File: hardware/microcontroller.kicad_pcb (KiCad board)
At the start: 2 copper layers, 50.8 x 78.7 mm, 77 parts, among them J5 1x2 jumper right-angle, J6 RJ45_Amphenol_RJMG1BD3B8K1ANR, J7 1x2 jumper right-angle, U1 W5500, U10 register file, U11 register file, U12 3.3V <=> 5V, U13 flip-flop, U14 3.3V <=> 5V, U15 decoder, U16 3.3V <=> 5V, U17 decoder, U2 3.3V <=> 5V, U3 counter, U4 counter, U5 counter, U6 counter, U7 counter, U8 shift register, U9 shift register, Y1 25MHz

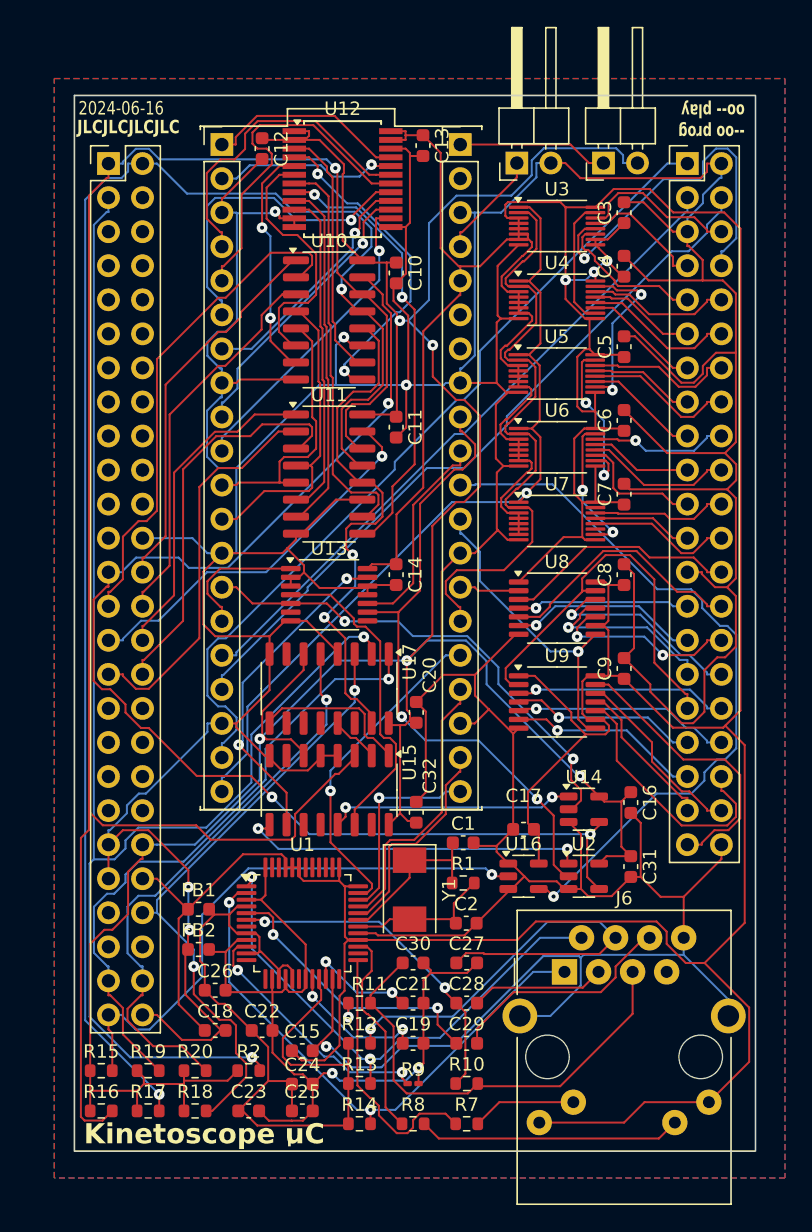
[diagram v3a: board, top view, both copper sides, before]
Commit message: Revise microcontroller board based on latest cart board improvements
 - Update comments
 - Segregate the Ethernet module's power supply so it can be
   disconnected if something goes wrong in a prototype
 - Update board setup to match latest cart board
 - Remove unnecessary level-shifter
 - Fix address decoder to non-latching version
 - Fix address decoder output assignment
 - Consolidate buffer ICs in register file
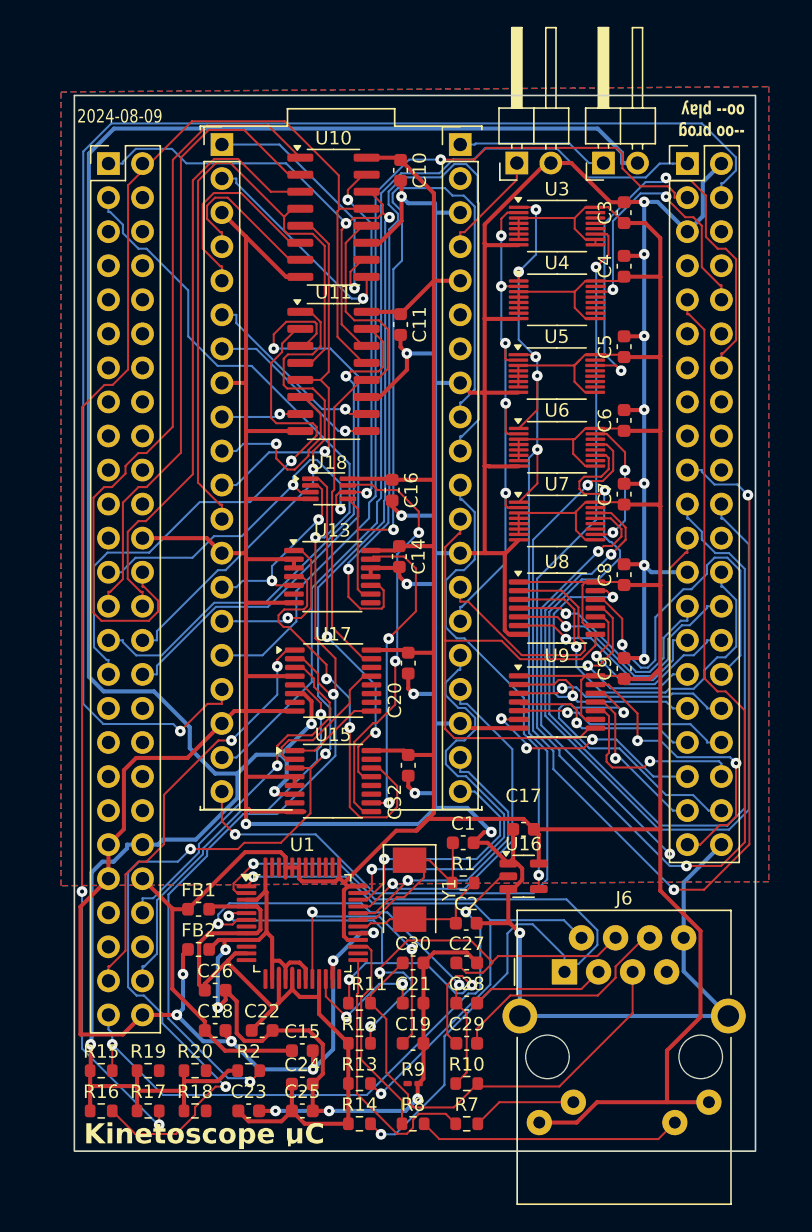
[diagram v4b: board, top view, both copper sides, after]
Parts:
- removed C12, C13, C31: 22nF, Capacitor_SMD:C_0603_1608Metric
- removed U12: 3.3V <=> 5V, Package_SO:SSOP-24_5.3x8.2mm_P0.65mm
- removed U14, U2: 3.3V <=> 5V, Package_TO_SOT_SMD:SOT-23-5
- added U18: 74LVC2G125, Package_SO:VSSOP-8_2.3x2mm_P0.5mm, F.Cu at (37.7, 48.6)
- U10, U11: value register file -> 74HC670
- U13: value flip-flop -> 74AHC74
- U15, U17: value decoder -> 74LVC138; footprint Package_SO:SO-16_3.9x9.9mm_P1.27mm -> Package_SO:TSSOP-16_4.4x5mm_P0.65mm
- U16: value 3.3V <=> 5V -> 74LV1T125
- U3, U4, U5, U6, U7: value counter -> 74LV163
- U8, U9: value shift register -> 74LV164
- moved C16 29.3 mm to (42.4, 48.7)
- moved C11 7.66 mm to (43.1, 36.4)
- moved U11 7.66 mm to (38.1, 39.9)
- moved C10 7.66 mm to (43.1, 24.9)
- moved U10 7.66 mm to (38.1, 28.4)
- moved C20 3.72 mm to (43.6, 61.6), turned to -90 degrees
- moved C32 3.55 mm to (43.6, 69.3), turned to -90 degrees
- moved C14 1.37 mm to (43.0, 53.7)
- moved U13 1.37 mm to (38.0, 55.2)
- moved U15 0.73 mm to (38.0, 70.4), turned to 0 degrees
- moved U17 0.67 mm to (38.0, 62.9), turned to 0 degrees
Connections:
- C10 pad 1: +5V -> +3.3V
- C11 pad 1: +5V -> +3.3V
- C16 pad 1: +5V -> +3.3V
- C20 pad 1: +5V -> +3.3V
- C32 pad 1: +5V -> +3.3V
- U10 pad 10: /register-file-internal/D_MID0 -> /REG_R_D0
- U10 pad 16: +5V -> +3.3V
- U10 pad 6: /register-file-internal/D_MID3 -> /REG_R_D3
- U10 pad 7: /register-file-internal/D_MID2 -> /REG_R_D2
- U10 pad 9: /register-file-internal/D_MID1 -> /REG_R_D1
- U11 pad 10: /register-file-internal/D_MID4 -> /REG_R_D4
- U11 pad 16: +5V -> +3.3V
- U11 pad 6: /register-file-internal/D_MID7 -> /REG_R_D7
- U11 pad 7: /register-file-internal/D_MID6 -> /REG_R_D6
- U11 pad 9: /register-file-internal/D_MID5 -> /REG_R_D5
- U15 pad 16: +5V -> +3.3V
- U17 pad 16: +5V -> +3.3V
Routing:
- net /address-counter-internal/A4: track 11.5 -> 103.3 mm, vias 0 -> 2
- net GND: track 537.5 -> 454.7 mm, vias 6 -> 22
- net /address-counter-internal/A14: track 7.64 -> 80.0 mm, vias 0 -> 3
- net /address-counter-internal/A16: track 9.47 -> 71.1 mm, vias 0 -> 1
- net +5V: track 216.9 -> 162.6 mm, vias 5 -> 3
- net /SRAM_DIS_2: track 54.6 -> 108.4 mm, vias 0 -> 1
- net /address-counter-internal/A17: track 10.1 -> 62.7 mm, vias 0 -> 1
- net /~{ERR_SET}: track 15.7 -> 66.5 mm, vias 0 -> 1
- net /address-counter-internal/A18: track 7.47 -> 57.5 mm, vias 0 -> 2
- net /SEGA_D0: track 94.0 -> 54.3 mm, vias 3 -> 4
- net /register-file-internal/D_MID5: track 33.2 -> 0.00 mm, vias 2 -> 0
- net /~{SRAM_W_A_CLR}: track 62.9 -> 93.4 mm, vias 1 -> 6
- net /register-file-internal/D_MID4: track 30.2 -> 0.00 mm
- net /SEGA_D1: track 28.5 -> 57.3 mm
- net /address-counter-internal/A3: track 27.7 -> 0.00 mm, vias 1 -> 0
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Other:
- board text added: "2024-08-09"
- board text removed: "2024-06-16"
- board text removed: "JLCJLCJLCJLC"

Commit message: Remove ethernet module, add pin header for Adafruit Ethernet featherwing instead
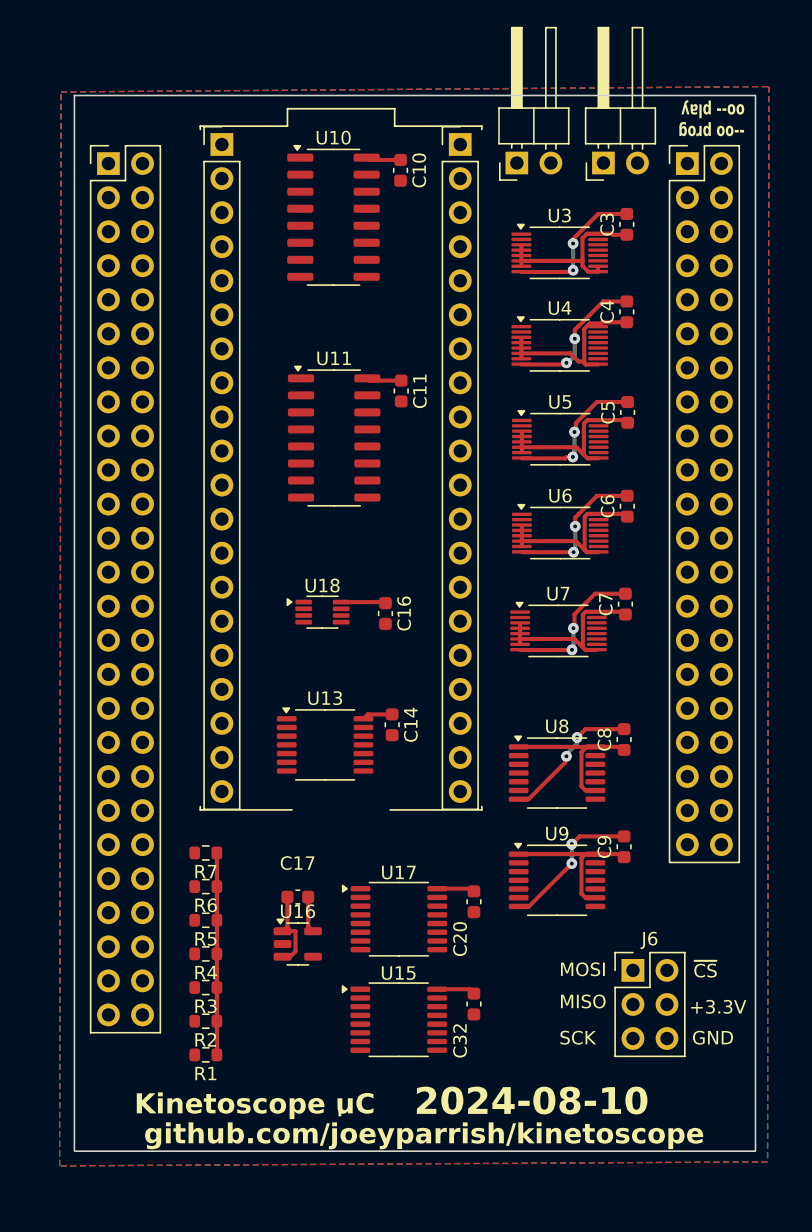
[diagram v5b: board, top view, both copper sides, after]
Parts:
- removed C1, C2: 22pF, Capacitor_SMD:C_0603_1608Metric
- removed C15, C19, C22: 10uF, Capacitor_SMD:C_0603_1608Metric
- removed C18, C21, C23, C24, C25, C26: 0.1uF, Capacitor_SMD:C_0603_1608Metric
- removed C27, C30: 10nF, Capacitor_SMD:C_0603_1608Metric
- removed C28, C29: 6.8nF, Capacitor_SMD:C_0603_1608Metric
- removed FB1, FB2: FerriteBead, Inductor_SMD:L_0603_1608Metric
- removed R10, R11, R13, R14: 49.9, Resistor_SMD:R_0603_1608Metric
- removed R12: 10, Resistor_SMD:R_0603_1608Metric
- removed R15, R16, R17, R18, R19, R20: 10k, Resistor_SMD:R_0603_1608Metric
- removed R8: 470, Resistor_SMD:R_0603_1608Metric
- removed R9: 12.4k 1%, Resistor_SMD:R_0201_0603Metric_Pad0.64x0.40mm_HandSolder
- removed U1: W5500, Package_QFP:LQFP-48_7x7mm_P0.5mm
- removed Y1: 25MHz, Crystal:Crystal_SMD_0603-2Pin_6.0x3.5mm
- added R3: 10k, Resistor_SMD:R_0603_1608Metric, F.Cu at (28.5, 85.8)
- added R4: 10k, Resistor_SMD:R_0603_1608Metric, F.Cu at (28.5, 83.3)
- added R5: 10k, Resistor_SMD:R_0603_1608Metric, F.Cu at (28.5, 80.8)
- added R6: 10k, Resistor_SMD:R_0603_1608Metric, F.Cu at (28.5, 78.3)
- J6: value RJ45_Amphenol_RJMG1BD3B8K1ANR -> Conn_02x03_Odd_Even; footprint Connector_RJ:RJ45_Amphenol_RJMG1BD3B8K1ANR -> Connector_PinHeader_2.54mm:PinHeader_2x03_P2.54mm_Vertical
- R1: value 1M -> 10k
- R7: value 470 -> 10k
- moved R7 28.0 mm to (28.5, 75.8), turned to 180 degrees
- moved R1 23.1 mm to (28.5, 90.9), turned to 180 degrees
- moved C20 18.5 mm to (48.5, 79.4)
- moved C32 18.5 mm to (48.5, 87.1)
- moved U15 18.5 mm to (42.9, 88.2)
- moved U17 18.5 mm to (42.9, 80.7)
- moved C17 17.6 mm to (35.4, 79.1)
- moved U16 17.6 mm to (35.4, 82.6)
- moved C9 13.3 mm to (59.7, 75.3)
- moved U9 13.3 mm to (54.7, 77.8)
- moved C14 12.6 mm to (42.4, 66.2)
- moved U13 12.6 mm to (37.4, 67.7)
- moved C8 12.3 mm to (59.7, 67.3)
- moved U8 12.3 mm to (54.7, 69.8)
- moved U18 9.21 mm to (37.2, 57.8)
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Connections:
- R1 pad 1: /ethernet-internal/XO -> +5V
- R1 pad 2: /ethernet-internal/XI -> /~{SEGA_RESET}
- R2 pad 2: /kinetoscope-header-internal/SEGA_A3 -> /kinetoscope-header-internal/SEGA_A1
- R7 pad 1: Net-(U1-LINKLED) -> +5V
- R7 pad 2: /ethernet-internal/GREEN_LED -> /~{SEGA_AS}
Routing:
- net GND: track 454.7 -> 82.8 mm, vias 22 -> 14
- net +3.3V: track 348.0 -> 112.7 mm
- net +5V: track 162.6 -> 15.1 mm, vias 3 -> 0
- net /kinetoscope-header-internal/SEGA_A1: track 131.3 -> 0.00 mm, vias 5 -> 0
- net /kinetoscope-header-internal/SEGA_A2: track 112.4 -> 0.00 mm, vias 2 -> 0
- net /SRAM_DIS_2: track 108.4 -> 0.00 mm, vias 1 -> 0
- net /address-counter-internal/A4: track 103.3 -> 0.00 mm, vias 2 -> 0
- net /~{SRAM_W_A_CLR}: track 93.4 -> 0.00 mm, vias 6 -> 0
- net /kinetoscope-header-internal/SEGA_A3: track 93.0 -> 0.00 mm, vias 3 -> 0
- net /address-counter-internal/A14: track 80.0 -> 0.00 mm, vias 3 -> 0
- net /~{SRAM_WE}: track 73.2 -> 0.00 mm
- net GNDA: track 71.2 -> 0.00 mm, vias 5 -> 0
- net /address-counter-internal/A16: track 71.1 -> 0.00 mm, vias 1 -> 0
- net /SRAM_DIS_1: track 68.0 -> 0.00 mm, vias 1 -> 0
- net /~{ERR_SET}: track 66.5 -> 0.00 mm, vias 1 -> 0
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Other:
- board text added: "+3.3V"
- board text added: "2024-08-10"
- board text added: "GND"
- board text added: "MISO"
- board text added: "MOSI"
- board text added: "SCK"
- board text added: "github.com/joeyparrish/kinetoscope"
- board text added: "~{CS}"
- board text removed: "2024-08-09"

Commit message: Revise microcontroller board based on latest cart board improvements
 - Update comments
 - Segregate the Ethernet module's power supply so it can be
   disconnected if something goes wrong in a prototype
 - Update board setup to match latest cart board
 - Remove unnecessary level-shifter
 - Fix address decoder to non-latching version
 - Fix address decoder output assignment
 - Consolidate buffer ICs in register file
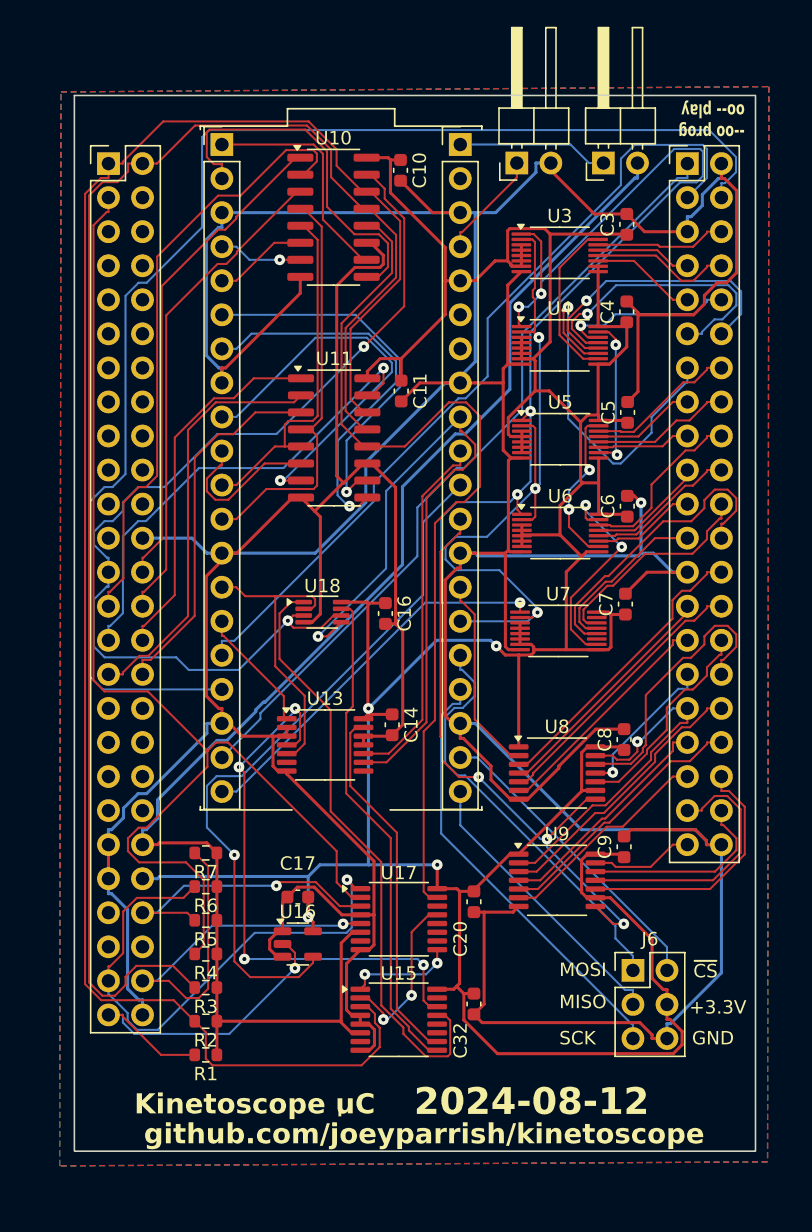
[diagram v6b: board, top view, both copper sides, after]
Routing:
- net GND: track 82.8 -> 487.9 mm, vias 14 -> 1
- net +3.3V: track 112.7 -> 286.7 mm, vias 0 -> 4
- net /kinetoscope-header-internal/SEGA_A1: track 0.00 -> 135.8 mm
- net /kinetoscope-header-internal/SEGA_A2: track 0.00 -> 115.8 mm
- net /~{SRAM_W_A_CLR}: track 0.00 -> 102.5 mm, vias 0 -> 5
- net /SRAM_DIS_2: track 0.00 -> 99.2 mm
- net +5V: track 15.1 -> 107.0 mm
- net /kinetoscope-header-internal/SEGA_A3: track 0.00 -> 87.7 mm
- net /SEGA_D0: track 0.00 -> 73.9 mm, vias 0 -> 2
- net /~{REG_WE}: track 0.00 -> 69.1 mm
- net /SRAM_DIS_1: track 0.00 -> 61.4 mm
- net /~{SRAM_WE}: track 0.00 -> 59.4 mm
- net /SRAM_W_A_CLK: track 0.00 -> 55.2 mm, vias 0 -> 3
- net /ERR_3V: track 0.00 -> 54.0 mm, vias 0 -> 1
- net /~{RESET_3V}: track 0.00 -> 52.6 mm, vias 0 -> 1
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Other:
- board text added: "2024-08-12"
- board text removed: "2024-08-10"
